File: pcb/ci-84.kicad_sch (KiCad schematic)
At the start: 120 parts, among them J1 Conn_01x02, SW1 SW_Push, SW10 XT0N, SW11 STAT, SW12 MATH, SW13 APPS, SW14 PRGM, SW15 VARS, SW16 CLEAR, SW17 X^-1, SW18 SIN, SW19 COS, SW2 Y=, SW20 TAN, SW21 ^, SW22 X^2, SW23 ,, SW24 (, SW25 ), SW26 DIVIDE, SW27 LOG, SW28 7, SW29 8, SW3 WINDOW, SW30 9, SW31 MULITPLY, SW32 IN, SW33 4, SW34 5, SW35 6, SW36 SUBTRACT, SW37 STO, SW38 1, SW39 2, SW4 ZOOM, SW40 3, SW41 ADD, SW42 ON, SW43 0, SW44 ., SW45 (-), SW46 ENTER, SW47 GRAPH, SW48 UP, SW49 RIGHT, SW5 TRACE, SW50 DOWN, SW51 LEFT, SW6 2ND, SW7 MODE, SW8 DEL, SW9 ALPHA, U1 STM32L471RGTx, U3 TPS63900, U4 TFT_320x240

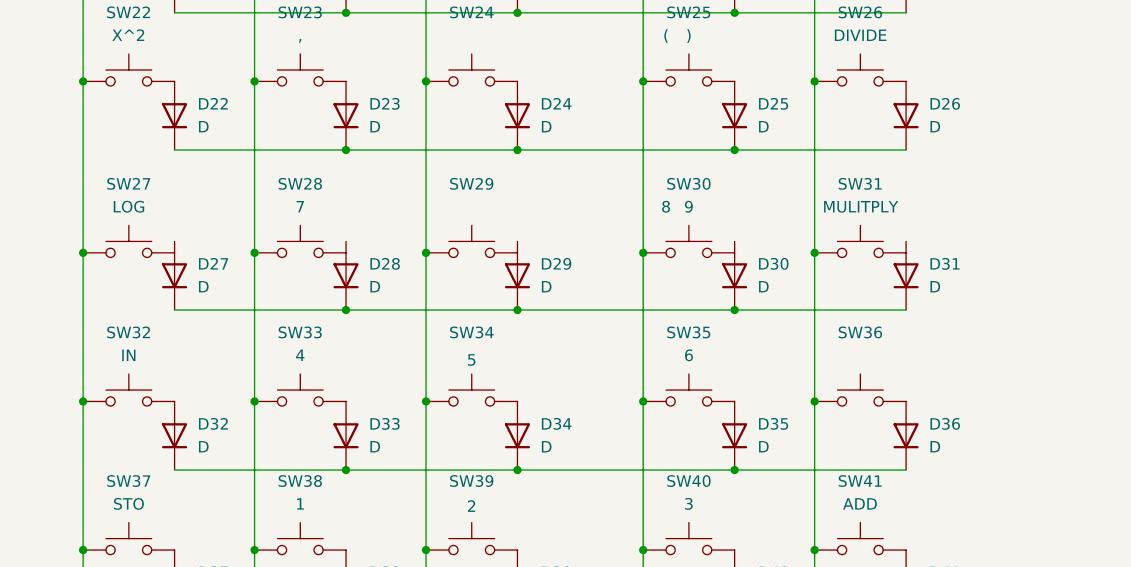
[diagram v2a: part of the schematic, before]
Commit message: finish keyboard diode matrix
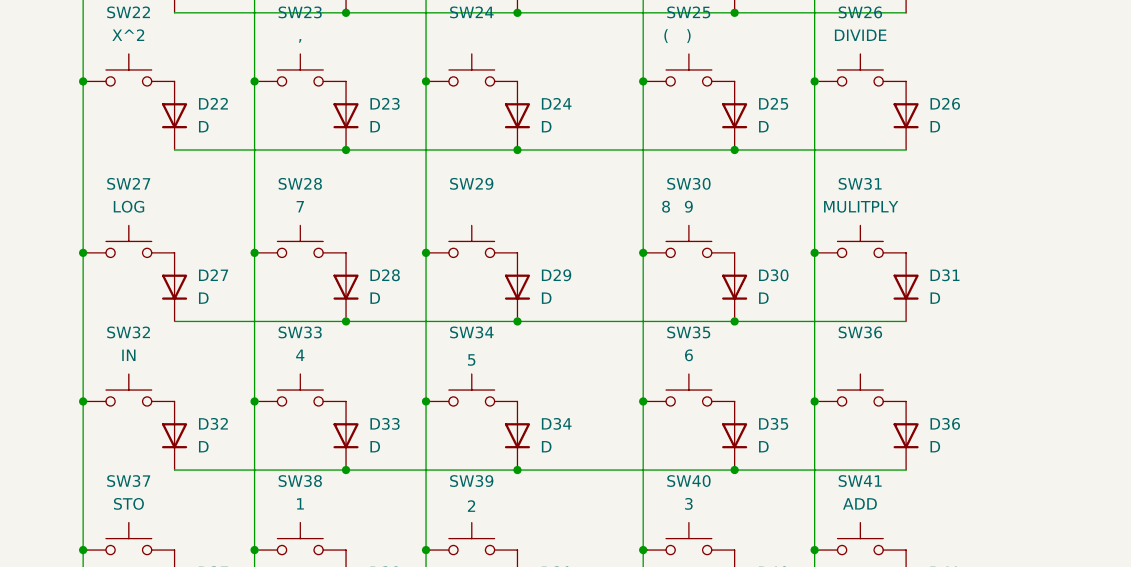
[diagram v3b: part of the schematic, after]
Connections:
- net at SW27.1: now also D27.2 (A)
- net at SW30.1: now also D30.2 (A)
- net at SW31.1: now also D31.2 (A)
- net at SW29.1: now also D29.2 (A)
- net at SW28.1: now also D28.2 (A)
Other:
- moved on the sheet: D27, D28, D29, D30, D31
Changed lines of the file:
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@@
 	)
 	(junction
-		(at 228.6 160.02)
+		(at 209.55 161.29)
 		(diameter 0)
 		(color 0 0 0 0)
@@
 	)
 	(junction
-		(at 209.55 160.02)
-		(diameter 0)
-		(color 0 0 0 0)
-	)
-	(junction
 		(at 228.6 212.09)
 		(diameter 0)
@@
 	)
 	(junction
+		(at 228.6 161.29)
+		(diameter 0)
+		(color 0 0 0 0)
+	)
+	(junction
 		(at 180.34 170.18)
 		(diameter 0)
@@
 	)
 	(junction
-		(at 252.73 160.02)
-		(diameter 0)
-		(color 0 0 0 0)
-	)
-	(junction
 		(at 59.69 52.07)
 		(diameter 0)
@@
 	)
 	(junction
+		(at 252.73 161.29)
+		(diameter 0)
+		(color 0 0 0 0)
+	)
+	(junction
 		(at 218.44 186.69)
 		(diameter 0)
@@
 	(wire
 		(pts
-			(xy 190.5 160.02) (xy 209.55 160.02)
+			(xy 190.5 161.29) (xy 209.55 161.29)
 		)
 		(stroke
@@
 	(wire
 		(pts
-			(xy 252.73 160.02) (xy 271.78 160.02)
-		)
-		(stroke
-			(width 0)
-			(type default)
-		)
-	)
-	(wire
-		(pts
 			(xy 261.62 153.67) (xy 261.62 170.18)
 		)
@@
 	(wire
 		(pts
-			(xy 190.5 68.58) (xy 209.55 68.58)
+			(xy 209.55 161.29) (xy 228.6 161.29)
 		)
 		(stroke
@@
 	(wire
 		(pts
-			(xy 209.55 160.02) (xy 228.6 160.02)
+			(xy 190.5 68.58) (xy 209.55 68.58)
 		)
 		(stroke
@@
 	(wire
 		(pts
+			(xy 228.6 161.29) (xy 252.73 161.29)
+		)
+		(stroke
+			(width 0)
+			(type default)
+		)
+	)
+	(wire
+		(pts
 			(xy 25.4 45.72) (xy 39.37 45.72)
 		)
@@
 	(wire
 		(pts
-			(xy 228.6 160.02) (xy 252.73 160.02)
+			(xy 180.34 186.69) (xy 180.34 204.47)
 		)
 		(stroke
@@
 	(wire
 		(pts
-			(xy 180.34 186.69) (xy 180.34 204.47)
+			(xy 228.6 142.24) (xy 252.73 142.24)
 		)
 		(stroke
@@
 	(wire
 		(pts
-			(xy 228.6 142.24) (xy 252.73 142.24)
+			(xy 252.73 161.29) (xy 271.78 161.29)
 		)
 		(stroke
@@
 	(symbol
 		(lib_id "Device:D")
-		(at 190.5 156.21 90)
+		(at 190.5 157.48 90)
 		(unit 1)
 		(exclude_from_sim no)
@@
 		(fields_autoplaced yes)
 		(property "Reference" "D27"
-			(at 193.04 154.9399 90)
+			(at 193.04 156.2099 90)
 			(effects
 				(font
@@
 		)
 		(property "Value" "D"
-			(at 193.04 157.4799 90)
+			(at 193.04 158.7499 90)
 			(effects
 				(font
@@
 		)
 		(property "Footprint" "Diode_SMD:D_SOD-123"
-			(at 190.5 156.21 0)
+			(at 190.5 157.48 0)
 			(effects
 				(font
@@
 		)
 		(property "Datasheet" "~"
-			(at 190.5 156.21 0)
+			(at 190.5 157.48 0)
 			(effects
 				(font
@@
 		)
 		(property "Description" "Diode"
-			(at 190.5 156.21 0)
+			(at 190.5 157.48 0)
 			(effects
 				(font
@@
 		)
 		(property "Sim.Device" "D"
-			(at 190.5 156.21 0)
+			(at 190.5 157.48 0)
 			(effects
 				(font
@@
 		)
 		(property "Sim.Pins" "1=K 2=A"
-			(at 190.5 156.21 0)
+			(at 190.5 157.48 0)
 			(effects
 				(font
@@
 	(symbol
 		(lib_id "Device:D")
-		(at 271.78 156.21 90)
+		(at 271.78 157.48 90)
 		(unit 1)
 		(exclude_from_sim no)
@@
 		(fields_autoplaced yes)
 		(property "Reference" "D31"
-			(at 274.32 154.9399 90)
+			(at 274.32 156.2099 90)
 			(effects
 				(font
@@
 		)
 		(property "Value" "D"
-			(at 274.32 157.4799 90)
+			(at 274.32 158.7499 90)
 			(effects
 				(font
@@
 		)
 		(property "Footprint" "Diode_SMD:D_SOD-123"
-			(at 271.78 156.21 0)
+			(at 271.78 157.48 0)
 			(effects
 				(font
@@
 		)
 		(property "Datasheet" "~"
-			(at 271.78 156.21 0)
+			(at 271.78 157.48 0)
 			(effects
 				(font
@@
 		)
 		(property "Description" "Diode"
-			(at 271.78 156.21 0)
+			(at 271.78 157.48 0)
 			(effects
 				(font
@@
 		)
 		(property "Sim.Device" "D"
-			(at 271.78 156.21 0)
+			(at 271.78 157.48 0)
 			(effects
 				(font
@@
 		)
 		(property "Sim.Pins" "1=K 2=A"
-			(at 271.78 156.21 0)
+			(at 271.78 157.48 0)
 			(effects
 				(font
@@
 	(symbol
 		(lib_id "Device:D")
-		(at 252.73 156.21 90)
+		(at 252.73 157.48 90)
 		(unit 1)
 		(exclude_from_sim no)
@@
 		(fields_autoplaced yes)
 		(property "Reference" "D30"
-			(at 255.27 154.9399 90)
+			(at 255.27 156.2099 90)
 			(effects
 				(font
@@
 		)
 		(property "Value" "D"
-			(at 255.27 157.4799 90)
+			(at 255.27 158.7499 90)
 			(effects
 				(font
@@
 		)
 		(property "Footprint" "Diode_SMD:D_SOD-123"
-			(at 252.73 156.21 0)
+			(at 252.73 157.48 0)
 			(effects
 				(font
@@
 		)
 		(property "Datasheet" "~"
-			(at 252.73 156.21 0)
+			(at 252.73 157.48 0)
 			(effects
 				(font
@@
 		)
 		(property "Description" "Diode"
-			(at 252.73 156.21 0)
+			(at 252.73 157.48 0)
 			(effects
 				(font
@@
 		)
 		(property "Sim.Device" "D"
-			(at 252.73 156.21 0)
+			(at 252.73 157.48 0)
 			(effects
 				(font
@@
 		)
 		(property "Sim.Pins" "1=K 2=A"
-			(at 252.73 156.21 0)
+			(at 252.73 157.48 0)
 			(effects
 				(font
@@
 	(symbol
 		(lib_id "Device:D")
-		(at 209.55 156.21 90)
+		(at 209.55 157.48 90)
 		(unit 1)
 		(exclude_from_sim no)
@@
 		(fields_autoplaced yes)
 		(property "Reference" "D28"
-			(at 212.09 154.9399 90)
+			(at 212.09 156.2099 90)
 			(effects
 				(font
@@
 		)
 		(property "Value" "D"
-			(at 212.09 157.4799 90)
+			(at 212.09 158.7499 90)
 			(effects
 				(font
@@
 		)
 		(property "Footprint" "Diode_SMD:D_SOD-123"
-			(at 209.55 156.21 0)
+			(at 209.55 157.48 0)
 			(effects
 				(font
@@
 		)
 		(property "Datasheet" "~"
-			(at 209.55 156.21 0)
+			(at 209.55 157.48 0)
 			(effects
 				(font
@@
 		)
 		(property "Description" "Diode"
-			(at 209.55 156.21 0)
+			(at 209.55 157.48 0)
 			(effects
 				(font
@@
 		)
 		(property "Sim.Device" "D"
-			(at 209.55 156.21 0)
+			(at 209.55 157.48 0)
 			(effects
 				(font
@@
 		)
 		(property "Sim.Pins" "1=K 2=A"
-			(at 209.55 156.21 0)
+			(at 209.55 157.48 0)
 			(effects
 				(font
@@
 	(symbol
 		(lib_id "Device:D")
-		(at 228.6 156.21 90)
+		(at 228.6 157.48 90)
 		(unit 1)
 		(exclude_from_sim no)
@@
 		(fields_autoplaced yes)
 		(property "Reference" "D29"
-			(at 231.14 154.9399 90)
+			(at 231.14 156.2099 90)
 			(effects
 				(font
@@
 		)
 		(property "Value" "D"
-			(at 231.14 157.4799 90)
+			(at 231.14 158.7499 90)
 			(effects
 				(font
@@
 		)
 		(property "Footprint" "Diode_SMD:D_SOD-123"
-			(at 228.6 156.21 0)
+			(at 228.6 157.48 0)
 			(effects
 				(font
@@
 		)
 		(property "Datasheet" "~"
-			(at 228.6 156.21 0)
+			(at 228.6 157.48 0)
 			(effects
 				(font
@@
 		)
 		(property "Description" "Diode"
-			(at 228.6 156.21 0)
+			(at 228.6 157.48 0)
 			(effects
 				(font
@@
 		)
 		(property "Sim.Device" "D"
-			(at 228.6 156.21 0)
+			(at 228.6 157.48 0)
 			(effects
 				(font
@@
 		)
 		(property "Sim.Pins" "1=K 2=A"
-			(at 228.6 156.21 0)
+			(at 228.6 157.48 0)
 			(effects
 				(font

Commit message: move arrow keys to keyboard matrix, add labels for riows
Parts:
- added D47, D48, D49, D50: D, Diode_SMD:D_SOD-123, symbol Device:D
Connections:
- net c5: now reaches SW16.2, SW21.2, SW26.2, SW31.2, SW36.2, SW41.2, SW46.2, SW47.2
- net c5: now also SW49.2, SW50.2
- net r4: now reaches D12.1 (K), D13.1 (K), D14.1 (K), D15.1 (K), D16.1 (K)
- net c1: now reaches SW12.2, SW17.2, SW2.1, SW22.2, SW27.2, SW32.2, SW37.2, SW42.2, SW6.2, SW9.2
- net r10: now reaches D42.1 (K), D43.1 (K), D44.1 (K), D45.1 (K), D46.1 (K)
- net r9: now reaches D37.1 (K), D38.1 (K), D39.1 (K), D40.1 (K), D41.1 (K)
- net r5: now reaches D17.1 (K), D18.1 (K), D19.1 (K), D20.1 (K), D21.1 (K)
- net c2: now reaches SW10.2, SW13.2, SW18.2, SW23.2, SW28.2, SW3.2, SW33.2, SW38.2, SW43.2, SW7.2
- net c3: now reaches SW11.2, SW14.2, SW19.2, SW24.2, SW29.2, SW34.2, SW39.2, SW4.2, SW44.2, SW8.2
- net r6: now reaches D22.1 (K), D23.1 (K), D24.1 (K), D25.1 (K), D26.1 (K)
- net at SW51.1: now also D47.2 (A)
- net c4: now reaches SW51.2
- net c4: now also SW15.2, SW20.2, SW25.2, SW30.2, SW35.2, SW40.2, SW45.2, SW48.2, SW5.2
- net r3: now reaches D10.1 (K), D11.1 (K), D9.1 (K)
- net r3: now also D47.1 (K), D49.1 (K)
- net r2: now reaches D6.1 (K), D7.1 (K), D8.1 (K)
- net r2: now also D48.1 (K), D50.1 (K)
- net r7: now reaches D27.1 (K), D28.1 (K), D29.1 (K), D30.1 (K), D31.1 (K)
- net r8: now reaches D32.1 (K), D33.1 (K), D34.1 (K), D35.1 (K), D36.1 (K)
- net at SW49.1: now also D50.2 (A)
- net r1: now reaches D1.1 (K), D2.1 (K), D3.1 (K), D4.1 (K), D5.1 (K)
- net at SW48.1: now also D48.2 (A)
- net at SW50.1: now also D49.2 (A)
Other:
- moved on the sheet: SW48, SW49, SW50, SW51

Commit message: wire matrix to mcirocontroller
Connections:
- net c1: now also U1.59 (PB7)
- net c2: now also U1.61 (PB8)
- net c3: now also U1.62 (PB9)
- net c4: now also U1.3 (PC14)
- net c5: now also U1.4 (PC15)
- net r1: now also U1.50 (PA15)
- net r10: now also U1.58 (PB6)
- net r2: now also U1.55 (PB3)
- net r3: now also U1.54 (PD2)
- net r4: now also U1.44 (PA11)
- net r5: now also U1.43 (PA10)
- net r6: now also U1.42 (PA9)
- net r7: now also U1.41 (PA8)
- net r8: now also U1.56 (PB4)
- net r9: now also U1.57 (PB5)
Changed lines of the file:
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@@
+		)
+	)
+	(label "r2"
+		(at 77.47 110.49 0)
+		(effects
+			(font
+				(size 1.27 1.27)
+			)
+			(justify left bottom)
+		)
+	)
+	(label "r7"
+		(at 77.47 80.01 0)
+		(effects
+			(font
+				(size 1.27 1.27)
+			)
+			(justify left bottom)
+		)
+	)
+	(label "c2"
+		(at 77.47 123.19 0)
+		(effects
+			(font
+				(size 1.27 1.27)
+			)
+			(justify left bottom)
 		)
 	)
@@
 		)
 	)
+	(label "r8"
+		(at 77.47 113.03 0)
+		(effects
+			(font
+				(size 1.27 1.27)
+			)
+			(justify left bottom)
+		)
+	)
 	(label "c5"
 		(at 261.62 41.91 180)
@@
 		)
 	)
+	(label "c1"
+		(at 77.47 120.65 0)
+		(effects
+			(font
+				(size 1.27 1.27)
+			)
+			(justify left bottom)
+		)
+	)
 	(label "c4"
 		(at 242.57 41.91 180)
@@
 		)
 	)
+	(label "c5"
+		(at 41.91 120.65 180)
+		(effects
+			(font
+				(size 1.27 1.27)
+			)
+			(justify right bottom)
+		)
+	)
 	(label "TS_CS"
 		(at 77.47 95.25 0)
@@
 		)
 	)
+	(label "r6"
+		(at 77.47 82.55 0)
+		(effects
+			(font
+				(size 1.27 1.27)
+			)
+			(justify left bottom)
+		)
+	)
 	(label "r8"
 		(at 271.78 177.8 0)
@@
 		)
 	)
+	(label "r10"
+		(at 77.47 118.11 0)
+		(effects
+			(font
+				(size 1.27 1.27)
+			)
+			(justify left bottom)
+		)
+	)
 	(label "SPI_CS"
 		(at 77.47 92.71 0)
@@
 		)
 	)
+	(label "r4"
+		(at 77.47 87.63 0)
+		(effects
+			(font
+				(size 1.27 1.27)
+			)
+			(justify left bottom)
+		)
+	)
+	(label "c3"
+		(at 77.47 125.73 0)
+		(effects
+			(font
+				(size 1.27 1.27)
+			)
+			(justify left bottom)
+		)
+	)
 	(label "TS_MISO"
 		(at 77.47 74.93 0)
@@
 		)
 	)
+	(label "r1"
+		(at 77.47 97.79 0)
+		(effects
+			(font
+				(size 1.27 1.27)
+			)
+			(justify left bottom)
+		)
+	)
 	(label "r10"
 		(at 271.78 212.09 0)
@@
 		)
 	)
+	(label "c4"
+		(at 41.91 118.11 180)
+		(effects
+			(font
+				(size 1.27 1.27)
+			)
+			(justify right bottom)
+		)
+	)
 	(label "IO_DC"
 		(at 139.7 80.01 0)
@@
 		)
 	)
+	(label "r3"
+		(at 41.91 77.47 180)
+		(effects
+			(font
+				(size 1.27 1.27)
+			)
+			(justify right bottom)
+		)
+	)
 	(label "r1"
 		(at 271.78 49.53 0)
@@
 		)
 	)
+	(label "r5"
+		(at 77.47 85.09 0)
+		(effects
+			(font
+				(size 1.27 1.27)
+			)
+			(justify left bottom)
+		)
+	)
 	(label "SCREEN_RST"
 		(at 139.7 82.55 0)
@@
 		(effects
 			(font
+				(size 1.27 1.27)
+			)
+			(justify left bottom)
+		)
+	)
+	(label "r9"
+		(at 77.47 115.57 0)
+		(effects
+			(font

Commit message: finish matrix connections
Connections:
- net c4: now also U1.4 (PC15); no longer U1.3 (PC14)
- net c5: now also U1.3 (PC14); no longer U1.4 (PC15)
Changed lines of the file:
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@@
 	)
 	(label "c5"
-		(at 41.91 120.65 180)
+		(at 41.91 118.11 180)
 		(effects
 			(font
@@
 	)
 	(label "c4"
-		(at 41.91 118.11 180)
+		(at 41.91 120.65 180)
 		(effects
 			(font

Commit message: finish wiring everthing
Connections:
- net IO_DC: now also U1.49 (PA14); no longer U1.2 (PC13)
- net IO_LED: now also U1.37 (PC6); no longer U1.40 (PC9)
- net SCREEN_RST: now also U1.39 (PC8); no longer U1.45 (PA12)
- net SPI3_MOSI: now also U1.52 (PC11); no longer U1.53 (PC12)
- net SPI3_SCK: now also U1.38 (PC7); no longer U1.51 (PC10)
- net SPI_CS: now also U1.40 (PC9); no longer U1.46 (PA13)
- net SPI_MISO: now also U1.53 (PC12); no longer U1.52 (PC11)
- net TS_CK: now also U1.36 (PB15); no longer U1.21 (PA5)
- net TS_CS: now also U1.35 (PB14); no longer U1.49 (PA14)
- net TS_MISO: now also U1.33 (PB12); no longer U1.22 (PA6)
- net TS_MOSI: now also U1.34 (PB13); no longer U1.23 (PA7)
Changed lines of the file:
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@@
 	)
 	(label "SPI_MISO"
-		(at 41.91 110.49 180)
+		(at 41.91 113.03 180)
 		(effects
 			(font
@@
 	)
 	(label "TS_MOSI"
-		(at 77.47 77.47 0)
+		(at 77.47 135.89 0)
 		(effects
 			(font
@@
 	)
 	(label "SPI3_SCK"
-		(at 41.91 107.95 180)
+		(at 41.91 100.33 180)
 		(effects
 			(font
@@
 	)
 	(label "SPI3_MOSI"
-		(at 41.91 113.03 180)
+		(at 41.91 110.49 180)
 		(effects
 			(font
@@
 	)
 	(label "TS_CS"
-		(at 77.47 95.25 0)
+		(at 77.47 138.43 0)
 		(effects
 			(font
@@
 	)
 	(label "SPI_CS"
-		(at 77.47 92.71 0)
-		(effects
-			(font
-				(size 1.27 1.27)
-			)
-			(justify left bottom)
-		)
-	)
-	(label "SPI_CS"
 		(at 139.7 85.09 0)
 		(effects
@@
 	)
 	(label "TS_MISO"
-		(at 77.47 74.93 0)
+		(at 77.47 133.35 0)
 		(effects
 			(font
@@
 	)
 	(label "SCREEN_RST"
-		(at 77.47 90.17 0)
-		(effects
-			(font
-				(size 1.27 1.27)
-			)
-			(justify left bottom)
+		(at 41.91 102.87 180)
+		(effects
+			(font
+				(size 1.27 1.27)
+			)
+			(justify right bottom)
 		)
 	)
@@
 	)
 	(label "IO_DC"
-		(at 41.91 115.57 180)
-		(effects
-			(font
-				(size 1.27 1.27)
-			)
-			(justify right bottom)
+		(at 77.47 95.25 0)
+		(effects
+			(font
+				(size 1.27 1.27)
+			)
+			(justify left bottom)
 		)
 	)
@@
 	)
 	(label "TS_CK"
-		(at 77.47 72.39 0)
+		(at 77.47 140.97 0)
 		(effects
 			(font
@@
 		)
 	)
+	(label "SPI_CS"
+		(at 41.91 105.41 180)
+		(effects
+			(font
+				(size 1.27 1.27)
+			)
+			(justify right bottom)
+		)
+	)
 	(label "TS_CK"
 		(at 139.7 67.31 0)
@@
 	)
 	(label "IO_LED"
-		(at 41.91 105.41 180)
-		(effects
-			(font
+		(at 41.91 97.79 180)
+		(effects
+			(font

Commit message: sheets for schematic
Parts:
- J1: value Conn_01x02 -> jst-battery
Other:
- added sheet Keyboard Matrix (keyboard.kicad_sch)
- added sheet Screen (screen.kicad_sch)
- added sheet Voltage Regulator (regulator.kicad_sch)
- added sheet stm32 (stm32.kicad_sch)
- note added: "battery for clock, memory retention"
- moved on the sheet: BT1, C1, C10, C11, C12, C2, C3, C4, C5, C6, C7, C8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
